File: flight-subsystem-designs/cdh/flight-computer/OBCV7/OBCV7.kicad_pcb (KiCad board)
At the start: 4 copper layers, 90.3 x 95.9 mm, 46 parts, among them U1 BEAGLEBONEBLACK, U3 TCAN337G, U4 MCP7940N-xSN, U5 ADM3485EARZ, U6 MAX706RESA+T, U7 TMP36xS

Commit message: It should be good this time guys trust
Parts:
- added G***: LOGO, LOGO, F.Cu at (166.7, 120.0)
- BT1: footprint Battery:BatteryHolder_Keystone_3034_1x20mm -> Battery:BatteryHolder_Keystone_106_1x20mm
- moved BT1 73.3 mm to (97.5, 69.0), turned to 0 degrees
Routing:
- net Net-(BT1-+): track 98.8 -> 62.4 mm, vias 1 -> 0
- net GND: track 91.6 -> 105.4 mm, vias 7 -> 6
- net Net-(C11-Pad1): track 201.3 -> 205.5 mm
- net SYS_5V: track 119.4 -> 121.4 mm
- net /CANH: track 52.5 -> 54.0 mm
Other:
- outline, holes or cut-outs redrawn
- board text added: "AVIONICS"
- board text added: "Flight Computer"
- board text added: "PULSE-A"
- board text added: "Rev. 7.0.0 - 6.2.26 - Gianni Alberico"
- board text added: "{dblquote}Im not playing on my phone, I'm taking care of business.{dblquote} -Eric Mays"

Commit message: obc changes'
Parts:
- U3: footprint Package_TO_SOT_SMD:TSOT-23-8 -> Footprints:TCAN337GD
- moved U3 3.01 mm to (126.3, 84.1)
- moved C2 2.98 mm to (132.7, 84.7)
- moved C5 2.98 mm to (132.6, 88.9)
- moved C1 2.98 mm to (132.7, 82.5)
- moved C3 2.98 mm to (132.7, 86.8)
- moved XTAL1 0.93 mm to (100.2, 109.1)
- renumbered WDO to TP1, OSC to TP2, GND to TP3
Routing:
- net Net-(U3-RXD): track 5.40 -> 12.5 mm
- net VDD_3V3B: track 66.3 -> 61.7 mm
- net Net-(U3-TXD): track 17.0 -> 21.4 mm
- net GND: track 105.4 -> 109.5 mm
- net Net-(C5-Pad1): track 17.0 -> 19.6 mm
- net /CANH: track 54.0 -> 56.0 mm
- net /I2C_SDA: track 259.0 -> 257.7 mm
- net /CAN_FAULT: track 47.2 -> 48.3 mm
- net /OSCVDD: track 7.37 -> 8.34 mm
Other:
- board text added: "3V3"
- board text added: "5V"

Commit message: idk
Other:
- board text added: "Rev. 7.0.0 - 6.11.26 - Gianni Alberico"
- board text removed: "Rev. 7.0.0 - 6.2.26 - Gianni Alberico"

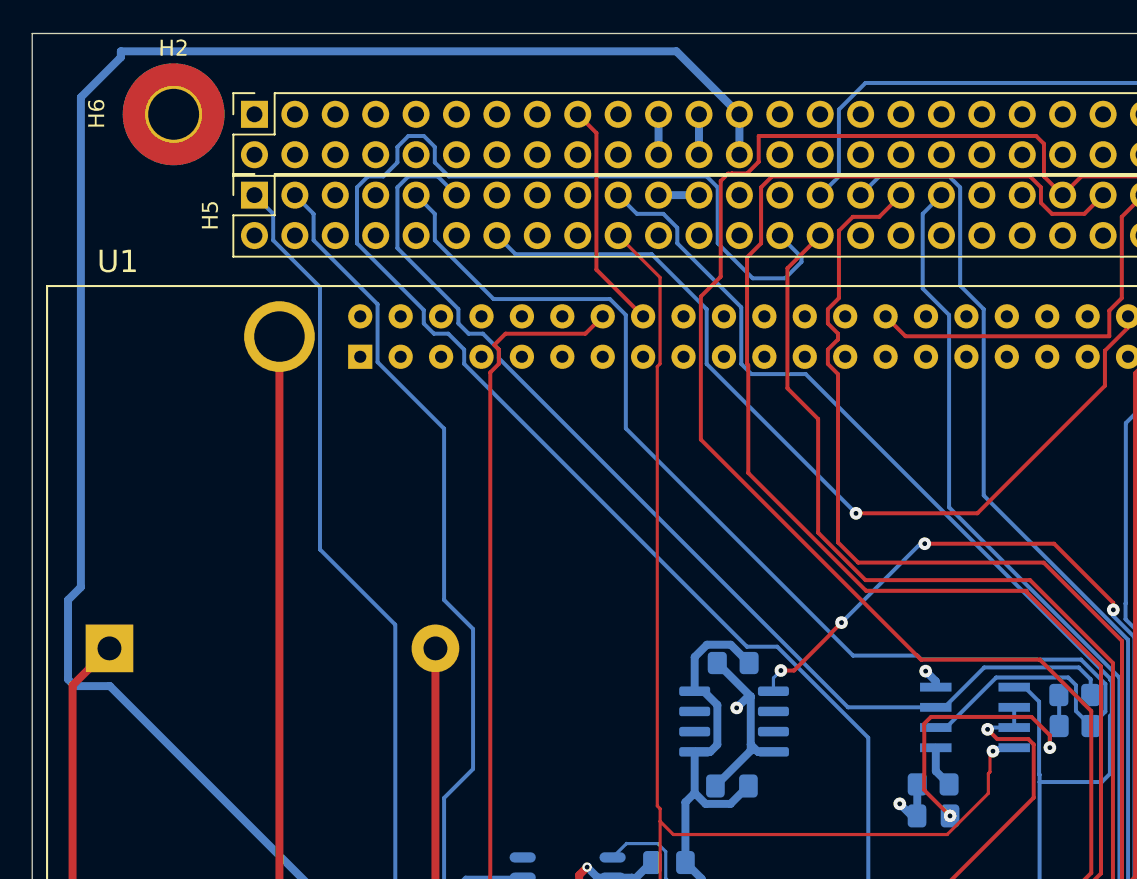
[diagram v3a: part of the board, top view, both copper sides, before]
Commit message: Fixed UART
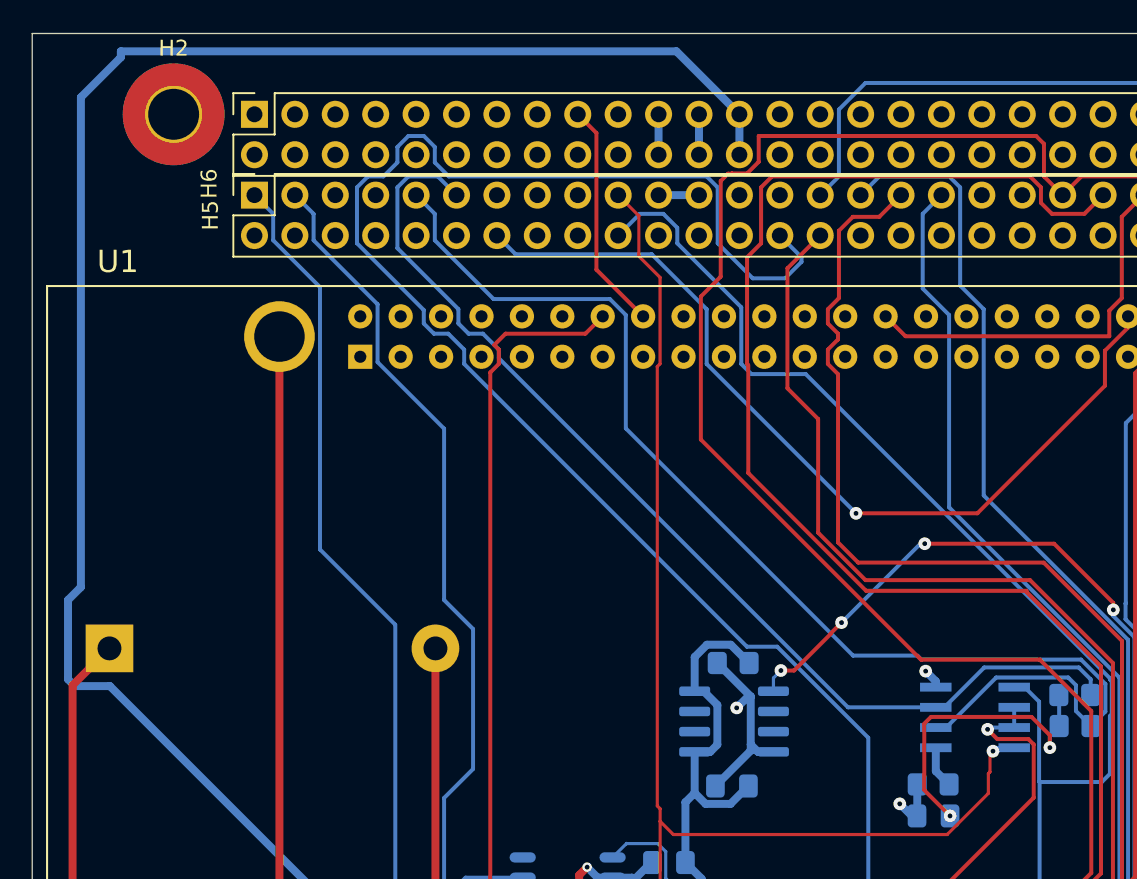
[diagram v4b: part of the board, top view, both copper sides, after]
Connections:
- H5 pad 19: /UART_RX -> /UART_TX
- H5 pad 20: /UART_TX -> /UART_RX
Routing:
- net /UART_TX: track 90.8 -> 93.3 mm

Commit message: New Footprint Fixes and Routing Improvements
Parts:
- removed the 3V3 at (121.7, 122.6)
- removed D2: 5V, LED_SMD:LED_0805_2012Metric
- removed D3: 3V3, LED_SMD:LED_0805_2012Metric
- removed TP1: WDO, TestPoint:TestPoint_THTPad_D3.0mm_Drill1.5mm
- removed TP2: CLKOUT, TestPoint:TestPoint_THTPad_D3.0mm_Drill1.5mm
- removed TP3: GND, TestPoint:TestPoint_THTPad_D3.0mm_Drill1.5mm
- removed U5: ADM3485EARZ, Footprints:R_8_ADI
- removed U7: TMP36xS, Package_SO:SOIC-8_3.9x4.9mm_P1.27mm
- added 3V3: TestPoint, TestPoint:TestPoint_THTPad_D3.0mm_Drill1.5mm, F.Cu at (107.4, 105.2)
- added 3V3: 3V3, LED_SMD:LED_0805_2012Metric, F.Cu at (176.8, 112.4)
- added 5V: 5V, LED_SMD:LED_0805_2012Metric, F.Cu at (176.8, 110.1)
- added GND: GND, TestPoint:TestPoint_THTPad_D3.0mm_Drill1.5mm, F.Cu at (107.4, 120.4)
- added OSC: CLKOUT, TestPoint:TestPoint_THTPad_D3.0mm_Drill1.5mm, F.Cu at (107.4, 115.3)
- added RS485: ADM3485EARZ, Footprints:R_8_ADI, F.Cu at (129.5, 104.7)
- added TMP36XS: TMP36xS, Package_SO:SOIC-8_3.9x4.9mm_P1.27mm, B.Cu at (136.7, 88.8)
- added WDO: WDO, TestPoint:TestPoint_THTPad_D3.0mm_Drill1.5mm, F.Cu at (107.4, 110.3)
- C1, C10, C3, C4, C9, R10, R11, R8, R9: moved to F.Cu
- U1: moved to B.Cu
- moved C11 54.2 mm to (171.7, 105.8), turned to 180 degrees
- moved R9 51.4 mm to (119.0, 107.1), turned to -90 degrees
- moved C8 51.3 mm to (163.9, 108.1), turned to 180 degrees
- moved R8 51.1 mm to (121.1, 107.1), turned to 90 degrees
- moved R10 49.9 mm to (99.2, 102.8)
- moved C9 49.7 mm to (164.0, 106.0)
- moved XTAL1 48.7 mm to (148.9, 111.4)
- moved U4 48.7 mm to (149.2, 107.2)
- moved C7 47.5 mm to (160.0, 101.9), turned to 180 degrees
- moved C12 46.8 mm to (164.0, 103.9), turned to 180 degrees
- moved C6 43.5 mm to (148.9, 102.6), turned to 0 degrees
- moved C1 41.8 mm to (163.9, 110.2)
- moved C3 40.3 mm to (163.9, 112.3)
- moved R1 38.9 mm to (150.2, 94.0), turned to 0 degrees
- moved D1 37.5 mm to (143.0, 104.2), turned to 0 degrees
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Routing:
- net /I2C_SDA: track 257.7 -> 94.3 mm
- net /I2C_SCL: track 171.8 -> 95.5 mm
- net /SPI_CSO: track 110.6 -> 57.1 mm
- net /PPS: track 55.8 -> 6.07 mm, vias 1 -> 0
- net Net-(U6-*WDO): track 9.43 -> 58.5 mm
- net /SPI_SCLK: track 114.0 -> 71.5 mm
- net SYS_5V: track 121.4 -> 86.0 mm
- net Net-(C11-Pad1): track 205.5 -> 238.6 mm, vias 2 -> 0
- net /UART2_RX: track 94.0 -> 61.6 mm
- net /SPI_D1: track 93.7 -> 63.0 mm
- net /Temp: track 61.7 -> 31.2 mm, vias 4 -> 0
- net /GPIO3_20: track 30.8 -> 59.1 mm, vias 1 -> 0
- net /RTCC_MFP: track 35.7 -> 8.90 mm, vias 1 -> 0
- net /GPIO1_17: track 41.9 -> 15.9 mm, vias 2 -> 0
- net Net-(U4-X1): track 25.8 -> 51.5 mm
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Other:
- board text removed: "3V3"
- board text removed: "5V"
